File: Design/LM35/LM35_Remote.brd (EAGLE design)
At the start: 100 x 80 mm, 9 parts

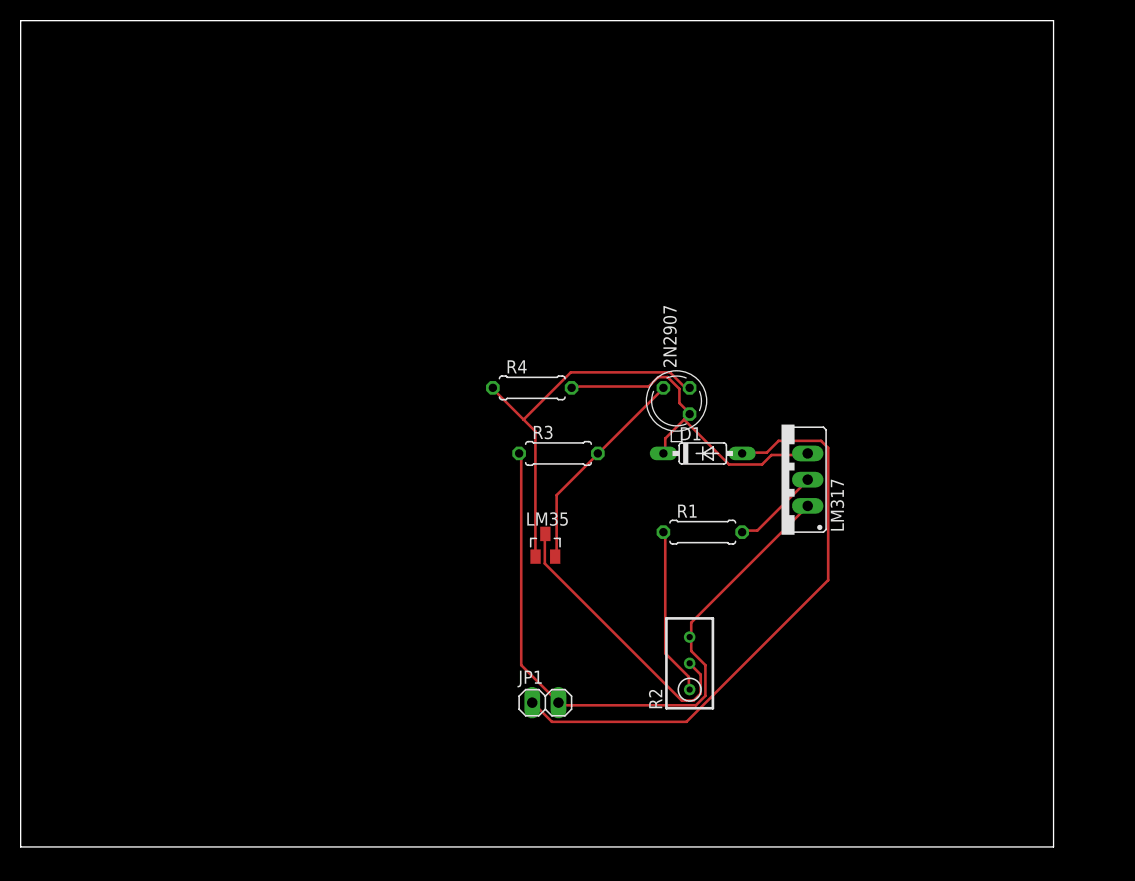
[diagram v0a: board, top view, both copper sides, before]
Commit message: Modificado el diseno de la  placa del sensor
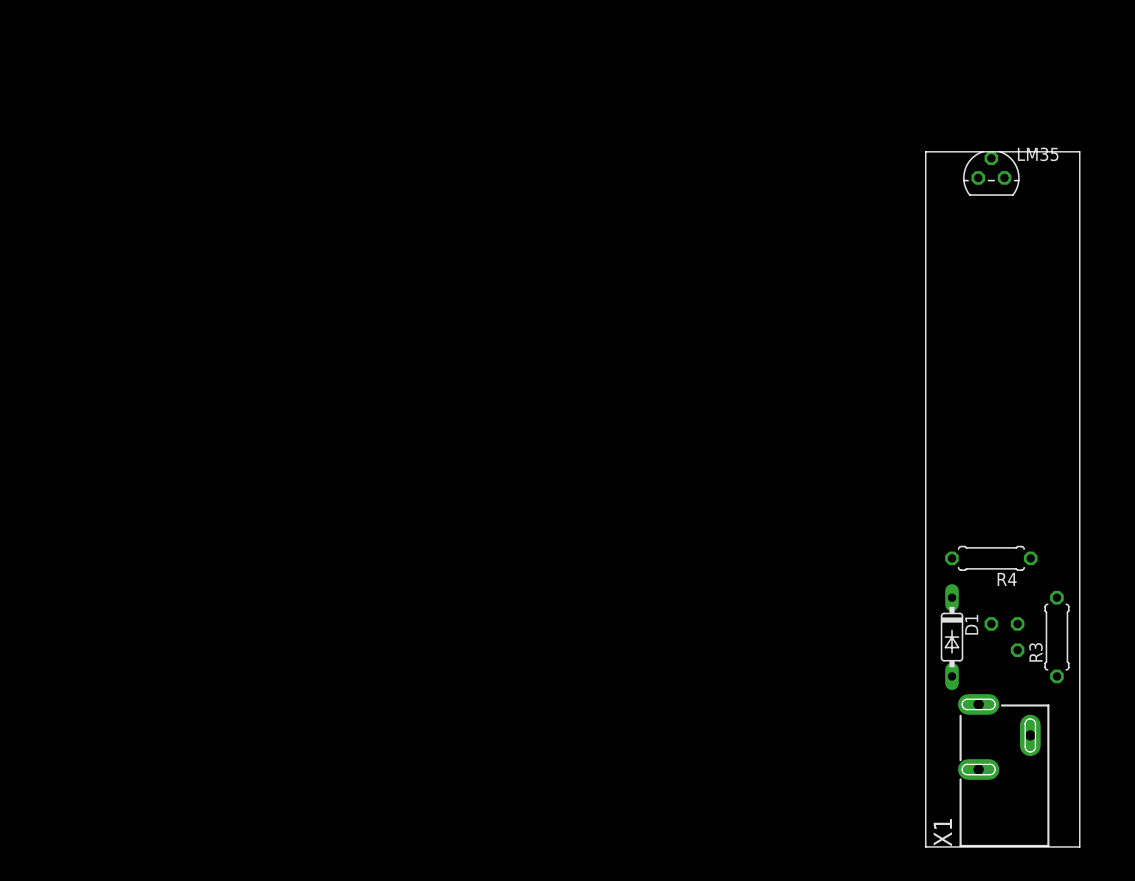
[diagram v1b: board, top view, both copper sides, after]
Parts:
- removed JP1: (no value), pinhead:1X02
- removed LM317: (no value), v-reg:317TS
- removed R1: 402, resistor:0207/7
- removed R2: 50, resistor:RTRIM3296W
- added X1: (no value), con-shiua-chyuan:SCD-014-A
- LM35: value LM50 -> LM35CZ; device linear:SOT23 -> lm35:TO92
- R3: value 62.5 -> 50-0.5%
- moved LM35 55.9 mm to (94.0, 64.8)
- moved R3 51.4 mm to (100.3, 20.3), turned to 90 degrees
- moved R4 47.4 mm to (94.0, 27.9), turned to 180 degrees
- moved 2N2907 39.1 mm to (95.2, 20.3), flipped to the bottom, turned to 180 degrees
- moved D1 30.0 mm to (90.2, 20.3), turned to 270 degrees
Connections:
- removed net N$6: LM317.2, R1.2
- removed net N$7: LM35.3, R2.2
- removed net N$8: D1.A, JP1.1
- net N$3: no longer LM317.3
- net N$4: now also LM35.3, X1.2, X1.3; no longer JP1.2, LM317.1, R2.3
- net N$5: now also D1.A, X1.1; no longer R1.1, R2.1
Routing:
- net N$4: track 64.2 -> 0.00 mm
- net N$8: track 57.0 -> 0.00 mm
- net N$1: track 36.7 -> 0.00 mm
- net N$3: track 33.3 -> 0.00 mm
- net N$7: track 27.1 -> 0.00 mm
- net N$2: track 20.8 -> 0.00 mm
- net N$5: track 16.3 -> 0.00 mm
- net N$6: track 8.49 -> 0.00 mm
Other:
- board size 100 x 80 mm -> 14.9 x 67.3 mm

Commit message: Ultima revision del resumen semanal
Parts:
- removed X1: (no value), con-shiua-chyuan:SCD-014-A
- added PLUG: (no value), con-shiua-chyuan:SCD-014-A
- moved 2N2907 6.35 mm to (95.2, 26.7), flipped to the top, turned to 0 degrees
- moved R4 6.35 mm to (94.0, 21.6)
- moved R3 5.68 mm to (95.2, 17.8), turned to 180 degrees
- moved LM35 4.02 mm to (95.2, 61.0), turned to 90 degrees
- moved D1 2.84 mm to (88.9, 17.8)
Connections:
- net N$4: now also PLUG.2, PLUG.3; no longer X1.2, X1.3
- net N$5: now also PLUG.1; no longer X1.1
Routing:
- net N$4: track 0.00 -> 67.6 mm
- net N$2: track 0.00 -> 59.1 mm
- net N$1: track 0.00 -> 44.7 mm
- net N$3: track 0.00 -> 7.12 mm
- net N$5: track 0.00 -> 2.75 mm
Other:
- board size 14.9 x 67.3 mm -> 17.5 x 63.5 mm
- board text added: "In: 12v"
- board text added: "PPS: Alvaro Alonso"
- board text added: "Temp: 0~100C (0~20mA)"
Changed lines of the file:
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@@
 <board>
 <plain>
-<wire x1="87.63" y1="0" x2="102.54" y2="0" width="0" layer="20"/>
-<wire x1="102.54" y1="0" x2="102.54" y2="67.3" width="0" layer="20"/>
-<wire x1="102.54" y1="67.3" x2="87.63" y2="67.3" width="0" layer="20"/>
-<wire x1="87.63" y1="67.3" x2="87.63" y2="0" width="0" layer="20"/>
+<wire x1="85.09" y1="0" x2="102.54" y2="0" width="0" layer="20"/>
+<wire x1="102.54" y1="0" x2="102.54" y2="63.49" width="0" layer="20"/>
+<wire x1="102.54" y1="63.49" x2="85.09" y2="63.49" width="0" layer="20"/>
+<wire x1="85.09" y1="63.49" x2="85.09" y2="0" width="0" layer="20"/>
+<text x="88.9" y="31.75" size="1.778" layer="1" rot="R90">Temp: 0~100C (0~20mA)</text>
+<text x="101.6" y="1.27" size="1.778" layer="1" rot="R90">In: 12v</text>
+<text x="101.6" y="35.56" size="1.778" layer="1" rot="R90">PPS: Alvaro Alonso</text>
+<dimension x1="85.09" y1="63.49" x2="85.09" y2="0" x3="80.01" y3="31.745" textsize="1.778" layer="1"/>
+<dimension x1="102.54" y1="63.49" x2="85.09" y2="63.49" x3="93.815" y3="67.31" textsize="1.778" layer="1"/>
 </plain>
 <attributes>
@@
 <classes>
 <class number="0" name="default" width="0" drill="0">
+<clearance class="0" value="0.205"/>
 </class>
 </classes>
-<designrules name="default">
+<designrules name="default *">
 <description language="de">&lt;b&gt;EAGLE Design Rules&lt;/b&gt;
 &lt;p&gt;
-Die Standard-Design-Rules sind so gewählt, dass sie für
+Die Standard-Design-Rules sind so gewÃÂ¤hlt, dass sie fÃÂ¼r
 die meisten Anwendungen passen. Sollte ihre Platine
 besondere Anforderungen haben, treffen Sie die erforderlichen
@@
 <param name="mtCopper" value="0.035mm 0.035mm 0.035mm 0.035mm 0.035mm 0.035mm 0.035mm 0.035mm 0.035mm 0.035mm 0.035mm 0.035mm 0.035mm 0.035mm 0.035mm 0.035mm"/>
 <param name="mtIsolate" value="1.5mm 0.15mm 0.2mm 0.15mm 0.2mm 0.15mm 0.2mm 0.15mm 0.2mm 0.15mm 0.2mm 0.15mm 0.2mm 0.15mm 0.2mm"/>
-<param name="mdWireWire" value="8mil"/>
-<param name="mdWirePad" value="8mil"/>
-<param name="mdWireVia" value="8mil"/>
-<param name="mdPadPad" value="8mil"/>
-<param name="mdPadVia" value="8mil"/>
-<param name="mdViaVia" value="8mil"/>
+<param name="mdWireWire" value="20mil"/>
+<param name="mdWirePad" value="20mil"/>
+<param name="mdWireVia" value="20mil"/>
+<param name="mdPadPad" value="20mil"/>
+<param name="mdPadVia" value="20mil"/>
+<param name="mdViaVia" value="20mil"/>
 <param name="mdSmdPad" value="8mil"/>
 <param name="mdSmdVia" value="8mil"/>
@@
 <param name="mdDrill" value="8mil"/>
 <param name="mdSmdStop" value="0mil"/>
-<param name="msWidth" value="10mil"/>
-<param name="msDrill" value="24mil"/>
+<param name="msWidth" value="30mil"/>
+<param name="msDrill" value="35mil"/>
 <param name="msMicroVia" value="9.99mm"/>
 <param name="msBlindViaRatio" value="0.5"/>
@@
 <autorouter>
 <pass name="Default">
-<param name="RoutingGrid" value="50mil"/>
+<param name="RoutingGrid" value="12.5mil"/>
 <param name="AutoGrid" value="1"/>
 <param name="Efforts" value="0"/>
 <param name="TopRouterVariant" value="1"/>
 <param name="tpViaShape" value="round"/>
-<param name="PrefDir.1" value="a"/>
+<param name="PrefDir.1" value="-"/>
 <param name="PrefDir.2" value="0"/>
 <param name="PrefDir.3" value="0"/>
@@
 </autorouter>
 <elements>
-<element name="2N2907" library="transistor" package="TO18" value="" x="95.25" y="20.32" rot="MR180"/>
-<element name="D1" library="diode" package="DO35-7" value="1N4148DO35-7" x="90.17" y="20.32" rot="R270"/>
-<element name="R3" library="resistor" package="0207/7" value="50-0.5%" x="100.33" y="20.32" rot="R90">
-<attribute name="SPICEPREFIX" value="R" x="100.33" y="20.32" size="1.778" layer="27" rot="R90" display="off"/>
+<element name="2N2907" library="transistor" package="TO18" value="" x="95.25" y="26.67"/>
+<element name="D1" library="diode" package="DO35-7" value="1N4148DO35-7" x="88.9" y="17.78" rot="R270"/>
+<element name="R3" library="resistor" package="0207/7" value="50-0.5%" x="95.25" y="17.78" rot="R180">
+<attribute name="SPICEPREFIX" value="R" x="95.25" y="17.78" size="1.778" layer="27" rot="R180" display="off"/>
 </element>
-<element name="R4" library="resistor" package="0207/7" value="4.7K" x="93.98" y="27.94" rot="R180">
-<attribute name="SPICEPREFIX" value="R" x="93.98" y="27.94" size="1.778" layer="27" rot="R180" display="off"/>
+<element name="R4" library="resistor" package="0207/7" value="4.7K" x="93.98" y="21.59" rot="R180">
+<attribute name="SPICEPREFIX" value="R" x="93.98" y="21.59" size="1.778" layer="27" rot="R180" display="off"/>
 </element>
-<element name="LM35" library="lm35" package="TO92" value="LM35CZ" x="93.98" y="64.77"/>
-<element name="X1" library="con-shiua-chyuan" package="SCD-014-A" value="" x="95.25" y="0">
-<attribute name="OC_NEWARK" value="unknown" x="95.25" y="0" size="1.778" layer="27" display="off"/>
-<attribute name="MPN" value="" x="95.25" y="0" size="1.778" layer="27" display="off"/>
-<attribute name="MF" value="" x="95.25" y="0" size="1.778" layer="27" display="off"/>
-<attribute name="OC_FARNELL" value="unknown" x="95.25" y="0" size="1.778" layer="27" display="off"/>
+<element name="LM35" library="lm35" package="TO92" value="LM35CZ" x="95.25" y="60.96" rot="R90"/>
+<element name="PLUG" library="con-shiua-chyuan" package="SCD-014-A" value="" x="93.98" y="0">
+<attribute name="OC_NEWARK" value="unknown" x="93.98" y="0" size="1.778" layer="27" display="off"/>
+<attribute name="MPN" value="" x="93.98" y="0" size="1.778" layer="27" display="off"/>
+<attribute name="MF" value="" x="93.98" y="0" size="1.778" layer="27" display="off"/>
+<attribute name="OC_FARNELL" value="unknown" x="93.98" y="0" size="1.778" layer="27" display="off"/>
 </element>
 </elements>
@@
 <contactref element="2N2907" pad="2"/>
 <contactref element="LM35" pad="1"/>
-<wire x1="97.79" y1="27.94" x2="92.71" y2="64.77" width="0" layer="19" extent="1-1"/>
-<wire x1="96.52" y1="21.59" x2="97.79" y2="27.94" width="0" layer="19" extent="1-1"/>
+<wire x1="97.79" y1="21.59" x2="99.06" y2="25.4" width="1.27" layer="1"/>
+<wire x1="99.06" y1="25.4" x2="99.06" y2="30.48" width="1.27" layer="1"/>
+<wire x1="96.52" y1="25.4" x2="99.06" y2="25.4" width="1.27" layer="1"/>
+<wire x1="99.06" y1="30.48" x2="95.25" y2="30.48" width="1.27" layer="1"/>
+<wire x1="95.25" y1="30.48" x2="95.25" y2="59.69" width="1.27" layer="1"/>
 </signal>
 <signal name="N$2">
@@
 <contactref element="R3" pad="2"/>
 <contactref element="LM35" pad="2"/>
-<wire x1="96.52" y1="19.05" x2="93.98" y2="66.675" width="0" layer="19" extent="1-1"/>
-<wire x1="100.33" y1="24.13" x2="96.52" y2="19.05" width="0" layer="19" extent="1-1"/>
+<wire x1="91.44" y1="17.78" x2="86.36" y2="17.78" width="1.27" layer="1"/>
+<wire x1="86.36" y1="17.78" x2="86.36" y2="27.94" width="1.27" layer="1"/>
+<wire x1="96.52" y1="27.94" x2="92.71" y2="27.94" width="1.27" layer="1"/>
+<wire x1="86.36" y1="27.94" x2="92.71" y2="27.94" width="1.27" layer="1"/>
+<wire x1="92.71" y1="27.94" x2="92.71" y2="60.96" width="1.27" layer="1"/>
+<wire x1="92.71" y1="60.96" x2="93.345" y2="60.96" width="1.27" layer="1"/>
 </signal>
 <signal name="N$3">
@@
 <contactref element="D1" pad="C"/>
 <contactref element="2N2907" pad="1"/>
-<wire x1="93.98" y1="21.59" x2="90.17" y2="27.94" width="0" layer="19" extent="1-1"/>
-<wire x1="90.17" y1="24.13" x2="93.98" y2="21.59" width="0" layer="19" extent="1-1"/>
+<wire x1="88.9" y1="21.59" x2="90.17" y2="21.59" width="1.27" layer="1"/>
+<wire x1="90.17" y1="21.59" x2="92.71" y2="25.4" width="1.27" layer="1"/>
+<wire x1="92.71" y1="25.4" x2="93.98" y2="25.4" width="1.27" layer="1"/>
 </signal>
 <signal name="N$4">
 <contactref element="R3" pad="1"/>
 <contactref element="LM35" pad="3"/>
-<contactref element="X1" pad="2"/>
-<contactref element="X1" pad="3"/>
-<wire x1="100.33" y1="16.51" x2="95.25" y2="64.77" width="0" layer="19" extent="1-1"/>
-<wire x1="97.75" y1="10.8" x2="100.33" y2="16.51" width="0" layer="19" extent="1-1"/>
-<wire x1="92.75" y1="7.5" x2="97.75" y2="10.8" width="0" layer="19" extent="1-1"/>
+<contactref element="PLUG" pad="2"/>
+<contactref element="PLUG" pad="3"/>
+<wire x1="91.48" y1="7.5" x2="96.48" y2="7.5" width="1.27" layer="1"/>
+<wire x1="96.48" y1="7.5" x2="96.48" y2="10.8" width="1.27" layer="1"/>
+<wire x1="96.48" y1="10.8" x2="99.06" y2="13.38" width="1.27" layer="1"/>
+<wire x1="99.06" y1="13.38" x2="99.06" y2="17.78" width="1.27" layer="1"/>
+<wire x1="99.06" y1="17.78" x2="101.6" y2="25.4" width="1.27" layer="1"/>
+<wire x1="101.6" y1="25.4" x2="101.6" y2="33.02" width="1.27" layer="1"/>
+<wire x1="101.6" y1="33.02" x2="97.79" y2="33.02" width="1.27" layer="1"/>
+<wire x1="97.79" y1="33.02" x2="97.79" y2="62.23" width="1.27" layer="1"/>
+<wire x1="97.79" y1="62.23" x2="95.25" y2="62.23" width="1.27" layer="1"/>
 </signal>
 <signal name="N$5">
 <contactref element="D1" pad="A"/>
-<contactref element="X1" pad="1"/>
-<wire x1="92.75" y1="13.8" x2="90.17" y2="16.51" width="0" layer="19" extent="1-1"/>
+<contactref element="PLUG" pad="1"/>
+<wire x1="91.48" y1="13.8" x2="88.9" y2="13.8" width="1.27" layer="1"/>
+<wire x1="88.9" y1="13.8" x2="88.9" y2="13.97" width="1.27" layer="1"/>
 </signal>
 </signals>

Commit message: Ultima modificacion plaqueta sensor
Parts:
- moved R3 86.4 mm to (8.89, 20.3), turned to 0 degrees
- moved LM35 84.3 mm to (11.4, 52.1), turned to 180 degrees
- moved PLUG 82.6 mm to (11.4, 1.27)
- moved 2N2907 82.5 mm to (12.7, 26.7), turned to 90 degrees
- moved R4 77.5 mm to (16.5, 24.1), turned to 270 degrees
- moved D1 76.2 mm to (12.7, 17.8), turned to 180 degrees
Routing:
- net N$2: track 59.1 -> 31.1 mm
- net N$1: track 44.7 -> 27.9 mm
- net N$4: track 67.6 -> 56.8 mm
- net N$3: track 7.12 -> 10.2 mm
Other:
- board size 17.5 x 63.5 mm -> 16.2 x 52.1 mm
- board text added: "Alvaro Alonso"
- board text added: "Sensor Temp. 5ºC/mA"
- board text removed: "In: 12v"
- board text removed: "PPS: Alvaro Alonso"
- board text removed: "Temp: 0~100C (0~20mA)"
